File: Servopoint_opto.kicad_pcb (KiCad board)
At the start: 2 copper layers, 60 x 61 mm, 33 parts, among them J1 TBP01R1-508-04BE, J2 TBP01R1-508-04BE, J3 Conn_01x05_Male, J5 Servo, J6 TBP01R1-508-03BE, J7 TBP01R1-508-03BE, Q1 BC847, Q2 BC847, U1 6N137, U2 LM2596S-5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

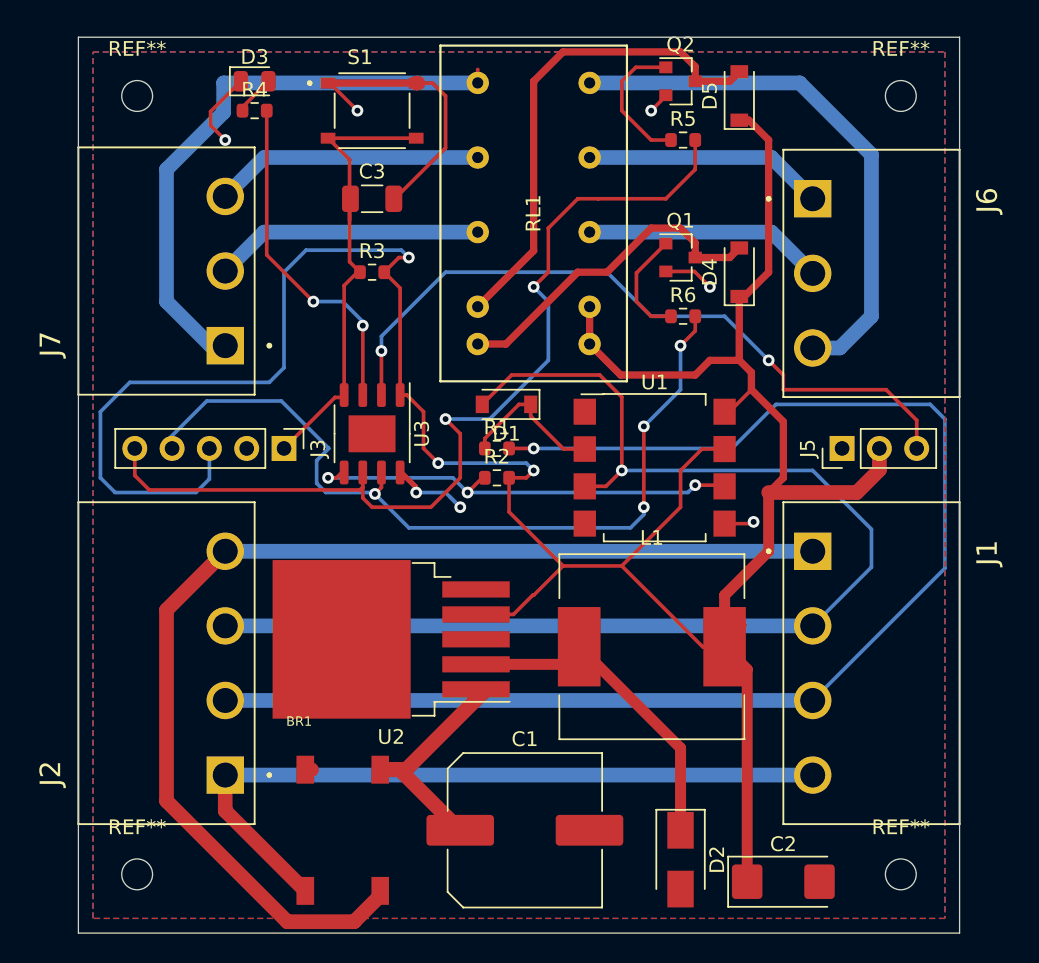
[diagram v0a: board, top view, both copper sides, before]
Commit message: changed pcb to 6 pin socket to programm pic via pickit 3, BOM and partnumber not updated yet, pcb not tested yet
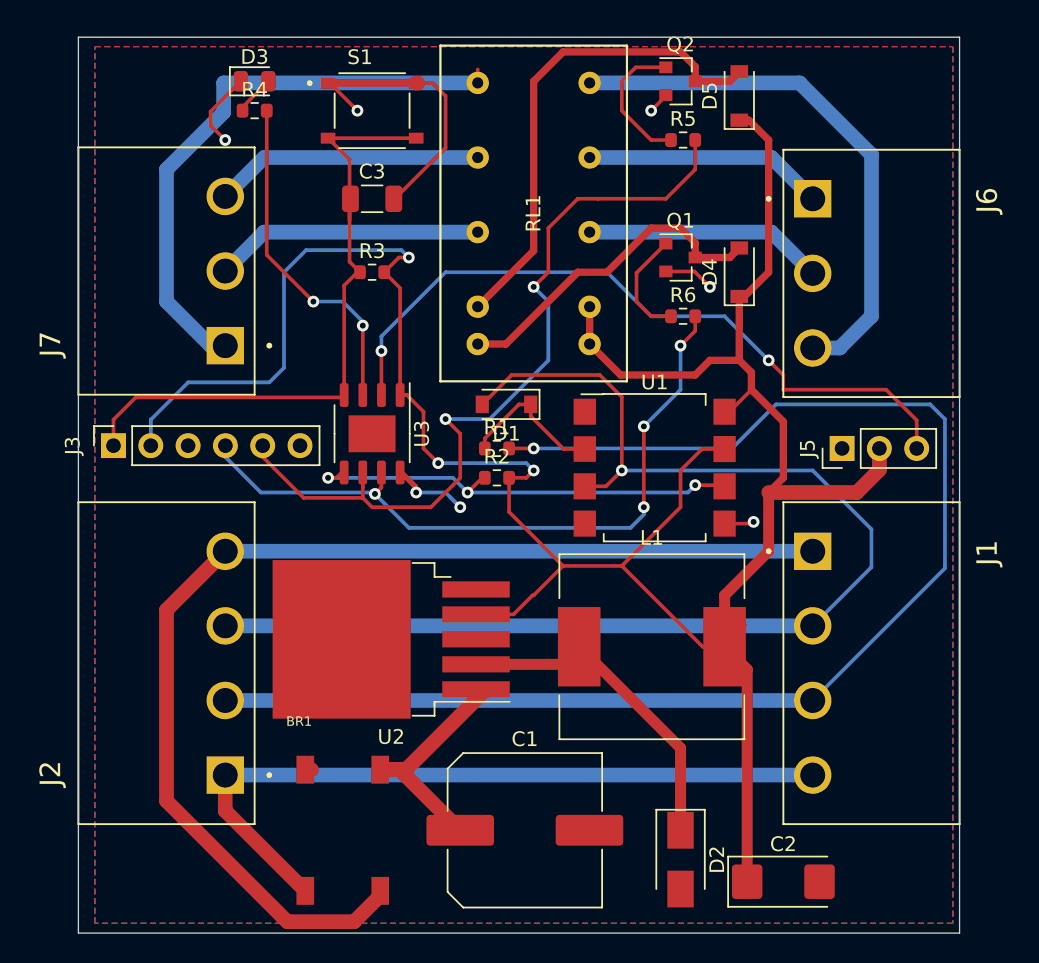
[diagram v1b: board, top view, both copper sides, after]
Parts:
- removed REF** (x4): MountingHole_2.1mm, MountingHole:MountingHole_2.1mm
- J3: value Conn_01x05_Male -> Conn_01x06_Male; footprint Connector_PinHeader_2.54mm:PinHeader_1x05_P2.54mm_Vertical -> Connector_PinSocket_2.54mm:PinSocket_1x06_P2.54mm_Vertical
- moved J3 11.6 mm to (72.4, 67.8), turned to 90 degrees
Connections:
- J3 pad 2: GND -> /Vdd
- J3 pad 3: /Vdd -> GND
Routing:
- net /Vdd: track 194.4 -> 178.1 mm
- net /Vpp: track 32.1 -> 44.7 mm
- net /Clk: track 64.0 -> 54.9 mm
- net /Data: track 57.2 -> 48.2 mm
